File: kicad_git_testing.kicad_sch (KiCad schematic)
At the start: 1 part

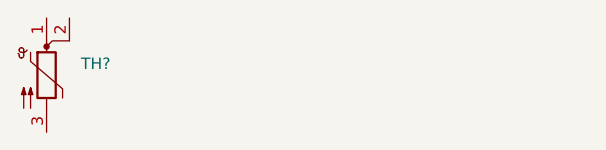
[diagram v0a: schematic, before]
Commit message: ADDed with capacitor and resistor
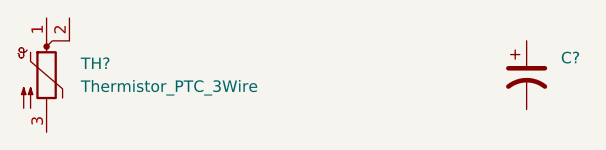
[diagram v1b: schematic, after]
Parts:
- added C?: (no value), symbol Device:C_Polarized_US
- TH?: value (none) -> Thermistor_PTC_3Wire
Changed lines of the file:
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@@
 (kicad_sch (version 20211123) (generator eeschema)
   (paper "A4")
+  (symbol (lib_id "Device:C_Polarized_US") (at 121.92 60.96 0) (unit 1)
+    (in_bom yes) (on_board yes) (fields_autoplaced)
+    (property "Reference" "C?" (id 0) (at 125.73 59.0549 0)
+      (effects (font (size 1.27 1.27)) (justify left))
+    )
+    (property "Value" "" (id 1) (at 125.73 61.5949 0)
+      (effects (font (size 1.27 1.27)) (justify left))
+    )
+    (property "Footprint" "" (id 2) (at 121.92 60.96 0)
+      (effects (font (size 1.27 1.27)) hide)
+    )
+    (property "Datasheet" "~" (id 3) (at 121.92 60.96 0)
+      (effects (font (size 1.27 1.27)) hide)
+    )
+    (pin "1")
+    (pin "2")
+  )
   (symbol (lib_id "Device:Thermistor_PTC_3Wire") (at 68.58 60.96 0) (unit 1)
     (in_bom yes) (on_board yes) (fields_autoplaced)
@@
       (effects (font (size 1.27 1.27)) (justify left))
     )
-    (property "Value" "" (id 1) (at 72.39 62.2299 0)
+    (property "Value" "Thermistor_PTC_3Wire" (id 1) (at 72.39 62.2299 0)
       (effects (font (size 1.27 1.27)) (justify left))
     )
@@
   )
   (symbol_instances
+    (path "/07838c19-bdee-4759-9a7b-a62a5deb9737"
+      (reference "C?") (unit 1) (value "C_Polarized_US") (footprint "")
+    )
     (path "/c454102f-dc92-4550-9492-797fc8e6b49c"
       (reference "TH?") (unit 1) (value "Thermistor_PTC_3Wire") (footprint "")

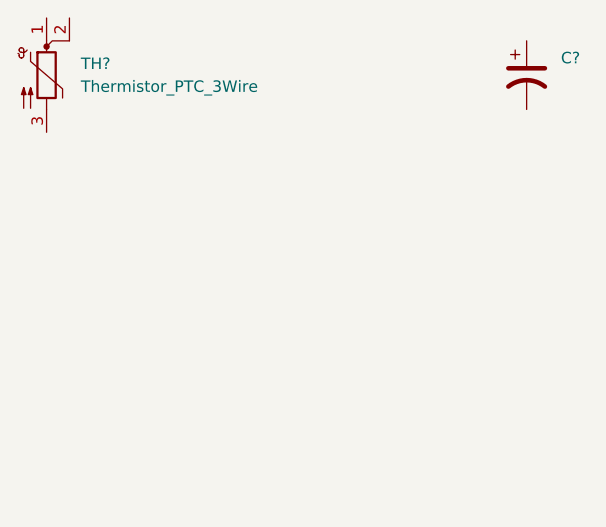
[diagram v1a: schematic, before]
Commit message: ADDed with capacitor and resistor and diode
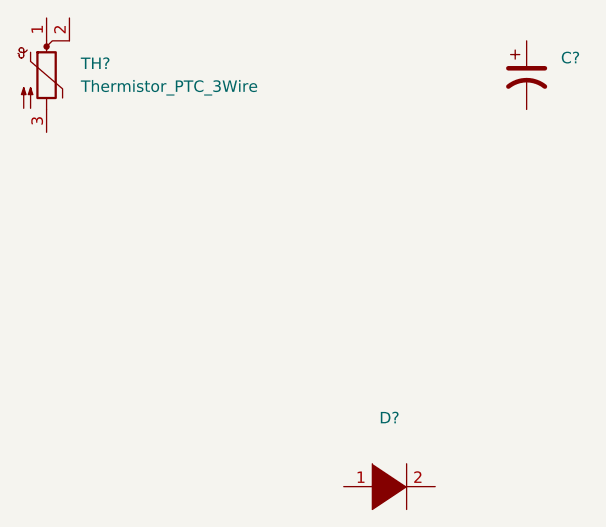
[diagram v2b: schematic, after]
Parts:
- added D?: (no value), symbol pspice:DIODE
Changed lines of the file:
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@@
+    (pin "2")
+  )
+  (symbol (lib_id "pspice:DIODE") (at 106.68 106.68 0) (unit 1)
+    (in_bom yes) (on_board yes) (fields_autoplaced)
+    (property "Reference" "D?" (id 0) (at 106.68 99.06 0))
+    (property "Value" "" (id 1) (at 106.68 101.6 0))
+    (property "Footprint" "" (id 2) (at 106.68 106.68 0)
+      (effects (font (size 1.27 1.27)) hide)
+    )
+    (property "Datasheet" "~" (id 3) (at 106.68 106.68 0)
+      (effects (font (size 1.27 1.27)) hide)
+    )
+    (pin "1")
     (pin "2")
   )
@@
       (reference "C?") (unit 1) (value "C_Polarized_US") (footprint "")
     )
+    (path "/4a5d9644-2379-4885-b4a6-a8623a813c99"
+      (reference "D?") (unit 1) (value "DIODE") (footprint "")
+    )
     (path "/c454102f-dc92-4550-9492-797fc8e6b49c"
